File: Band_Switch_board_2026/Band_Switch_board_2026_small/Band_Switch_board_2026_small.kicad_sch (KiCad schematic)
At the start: 29 parts, among them J1 KMDGX-8S-N, J2 AUX Out, J3 PTT Rig, J4 ICOM Band, J5 I2C Bus, J6 AUX Out, J7 PTT, J8 ADC Module, U1 ADS1015IDGS

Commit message: delete files
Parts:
- J8: value ADC Module -> ADC Module Option
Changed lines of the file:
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@@
 			)
 		)
-		(property "Value" "ADC Module"
+		(property "Value" "ADC Module Option"
 			(at 118.11 138.4299 0)
 			(effects

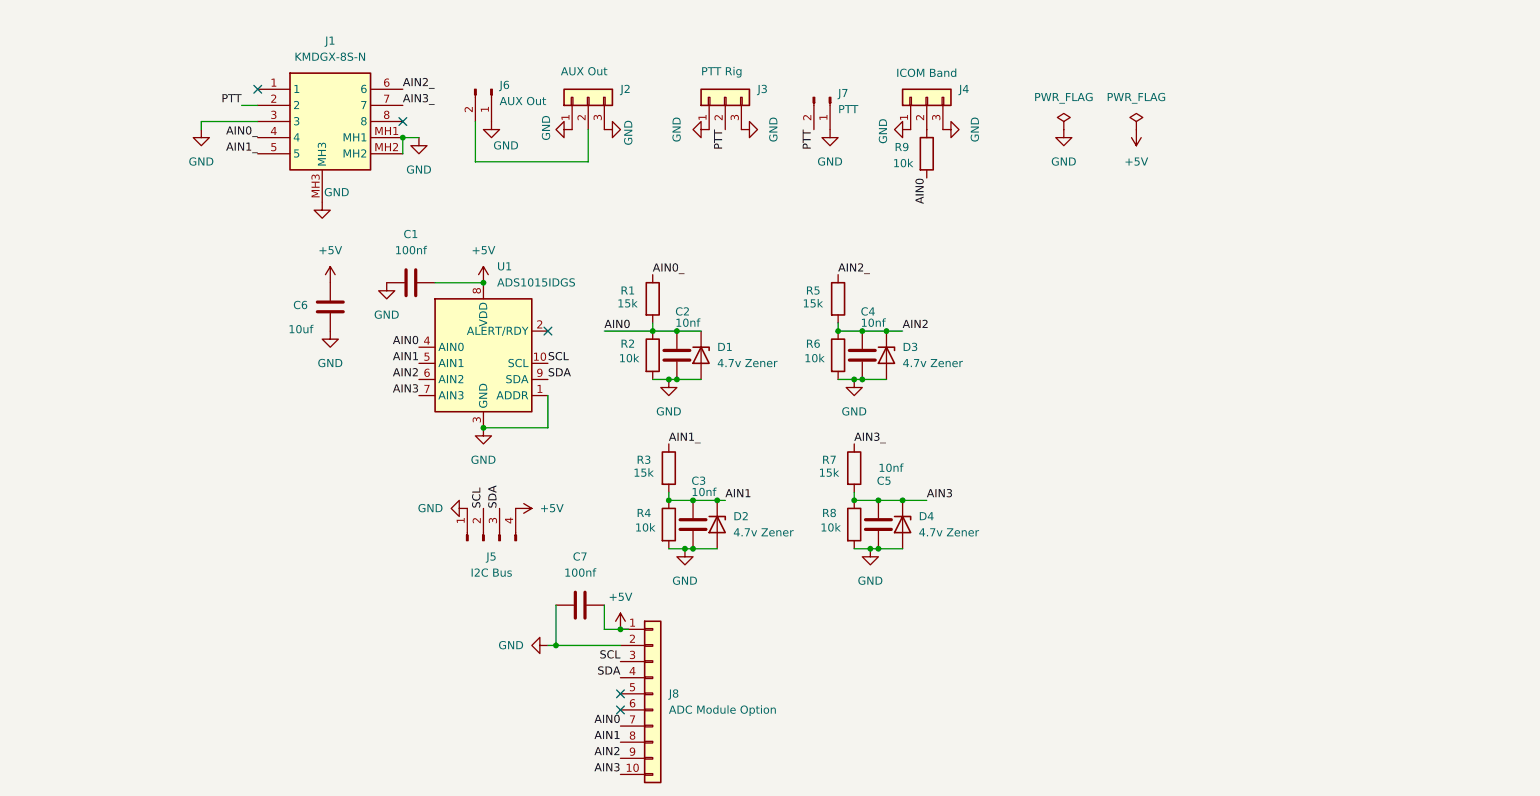
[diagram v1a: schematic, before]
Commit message: update pcb files to kicad 10
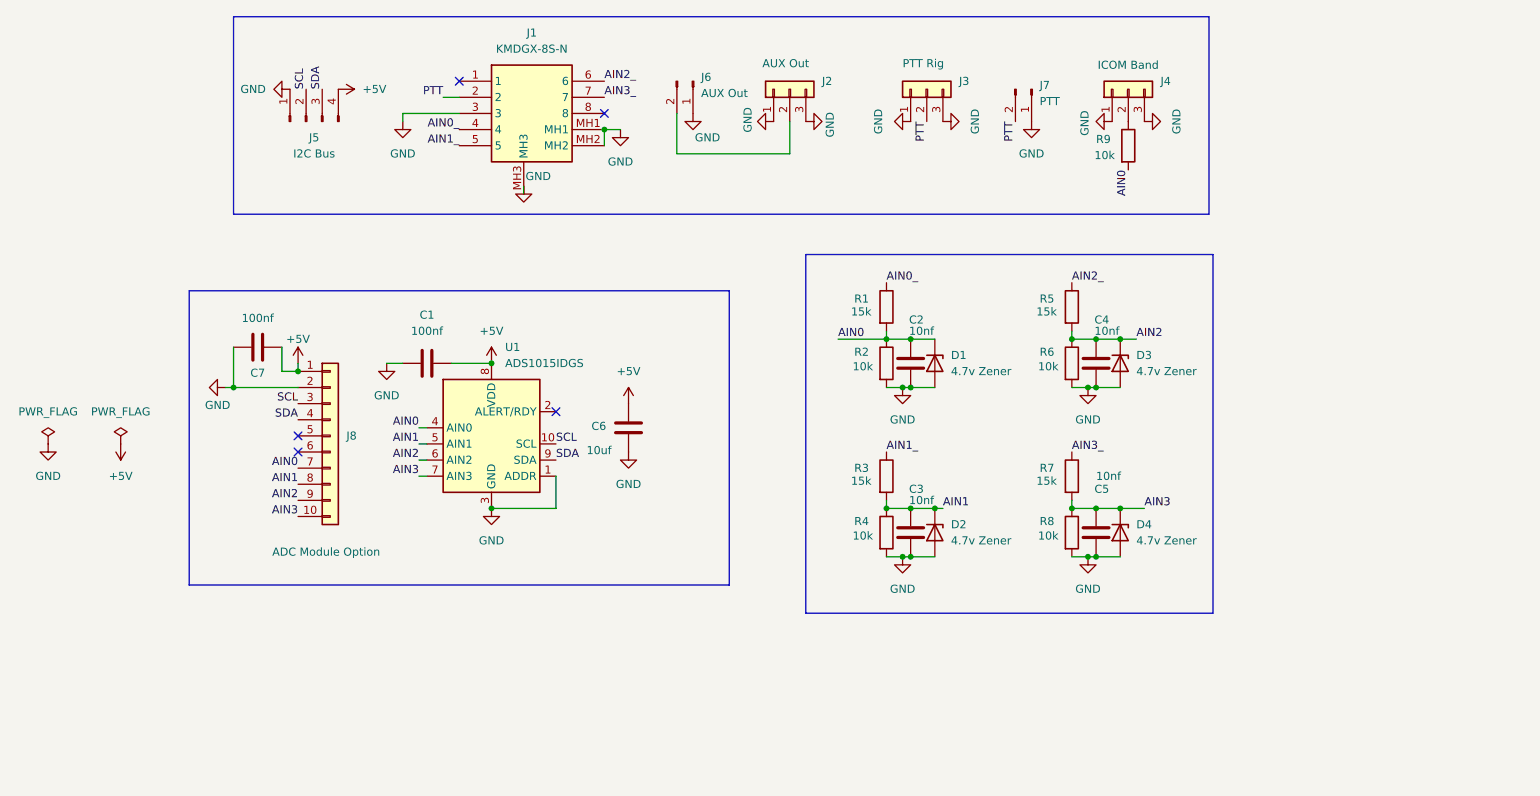
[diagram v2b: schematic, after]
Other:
- moved on the sheet: C1, C2, C3, C4, C5, C6, C7, D1, D2, D3, D4, J1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

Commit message: change some values - alter boards
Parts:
- added C8: 100nf, Capacitor_THT:C_Disc_D6.0mm_W2.5mm_P5.00mm, symbol Device:C
- added U2: 24LC32, Package_DIP:DIP-8_W7.62mm_Socket, symbol Memory_EEPROM:24LC32
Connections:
- net +5V: now also C8.2, U2.8 (VCC)
- net GND: now also C8.1, U2.1 (A0), U2.2 (A1), U2.3 (A2), U2.4 (GND), U2.7 (WP)
- net SCL: now also U2.6 (SCL)
- net SDA: now also U2.5 (SDA)
